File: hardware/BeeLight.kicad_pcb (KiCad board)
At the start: 2 copper layers, 32 x 24 mm, 25 parts, among them IC102 APDS-9306-065, IC103 BME688, M101 BL54L15, Q101 BSS84, SW101 JOIN, X102 DEBUG

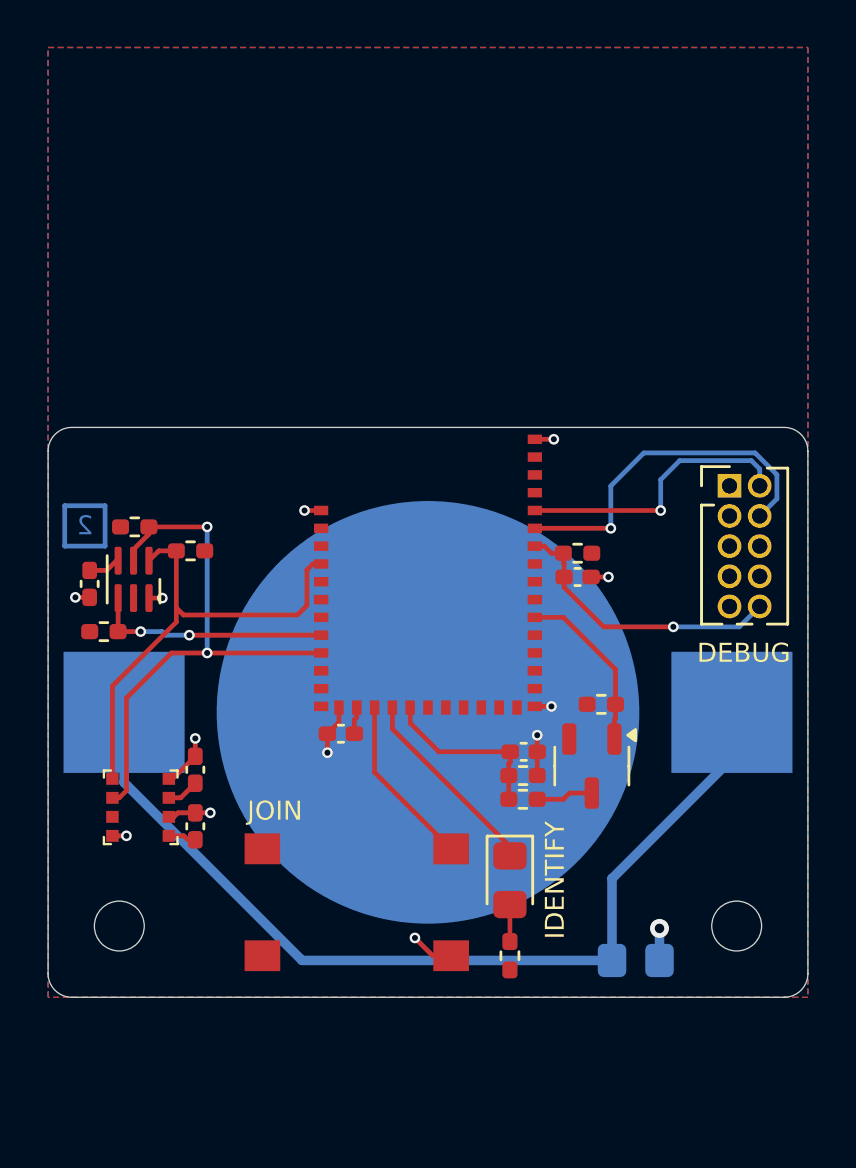
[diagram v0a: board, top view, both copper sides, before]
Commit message: Feature: Issue #28
- Switch from CR2032 to CR2477 batteries for longer runtime

Closes #28

Signed-off-by: Daniel Kampert <DanielKampert@kampis-elektroecke.de>
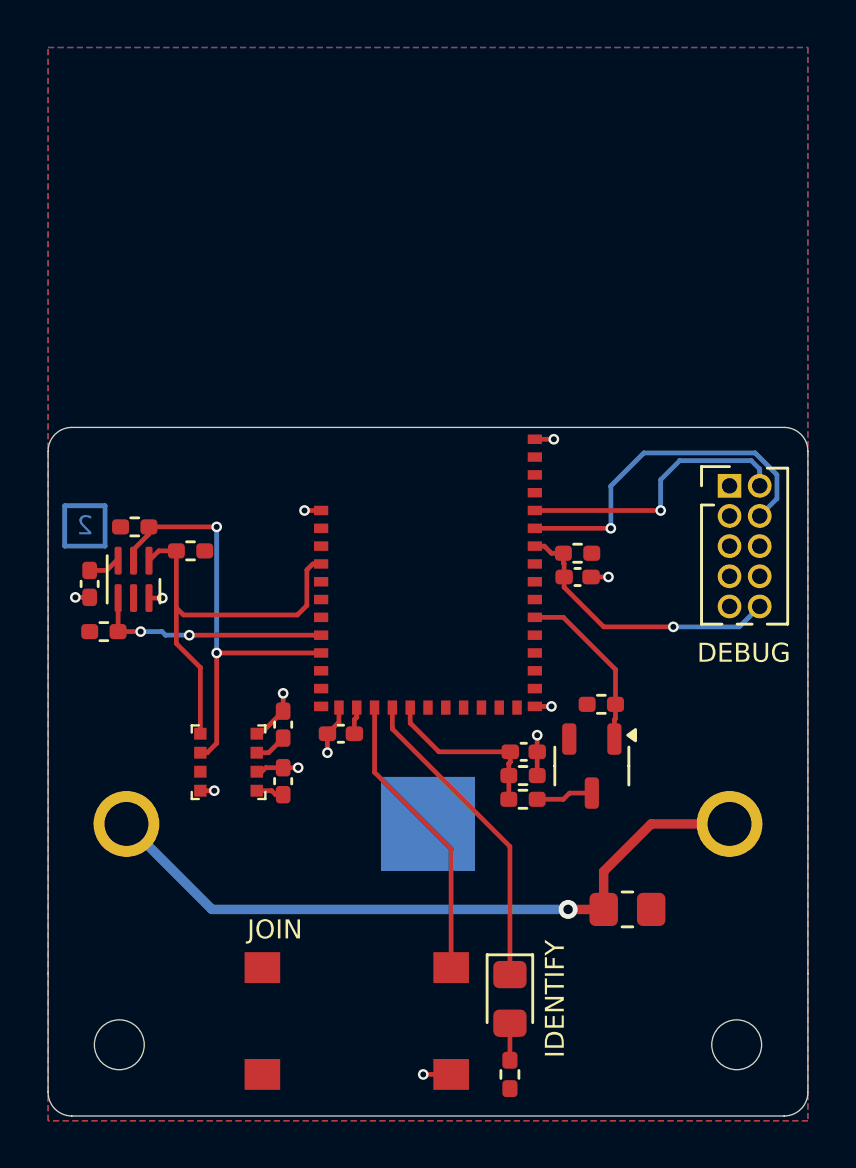
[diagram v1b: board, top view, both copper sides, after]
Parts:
- removed the REF** at (125.0, 103.0)
- removed the REF** at (151.0, 103.0)
- added REF**: MountingHole_2.1mm, MountingHole:MountingHole_2.1mm, F.Cu at (151.0, 108.0)
- added REF**: MountingHole_2.1mm, MountingHole:MountingHole_2.1mm, F.Cu at (125.0, 108.0)
- BT101: footprint Keystone:3002 -> Keystone:3039
- R102: moved to F.Cu
- moved D101 5.00 mm to (141.4, 106.1)
- moved R103 5.00 mm to (141.4, 109.2)
- moved SW101 5.00 mm to (135.0, 107.0)
- moved BT101 4.70 mm to (138.0, 98.7)
- moved C106 4.16 mm to (131.9, 94.5)
- moved C105 4.16 mm to (131.9, 96.9)
- moved IC103 4.16 mm to (129.6, 96.1)
- moved R102 2.18 mm to (146.4, 102.3)
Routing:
- net Net-(BT101-+): track 39.1 -> 29.3 mm, vias 0 -> 1
- net Net-(M101-P1.00/32K): track 7.29 -> 12.3 mm
- net Net-(D101-K): track 8.30 -> 13.3 mm
- net SDA: track 23.1 -> 18.9 mm
- net SCL: track 20.0 -> 17.4 mm
- net +BATT: track 6.41 -> 5.06 mm, vias 1 -> 0
- net GND: track 14.4 -> 13.7 mm
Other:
- board size 32 x 24 mm -> 32 x 29 mm
